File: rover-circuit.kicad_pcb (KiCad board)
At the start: 2 copper layers, 78 x 75.3 mm, 86 parts, among them J1 Battery Connector, J2 USB_C_Receptacle_USB2.0_14P, J3 Conn_01x04, J4 Conn_01x04_Socket, J5 Raspberry_Pi_2_3, J6 Conn_02x07_Odd_Even, M1 Motor_DC, M2 Motor_DC, SW1 SW_EN, SW2 SW_IO0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

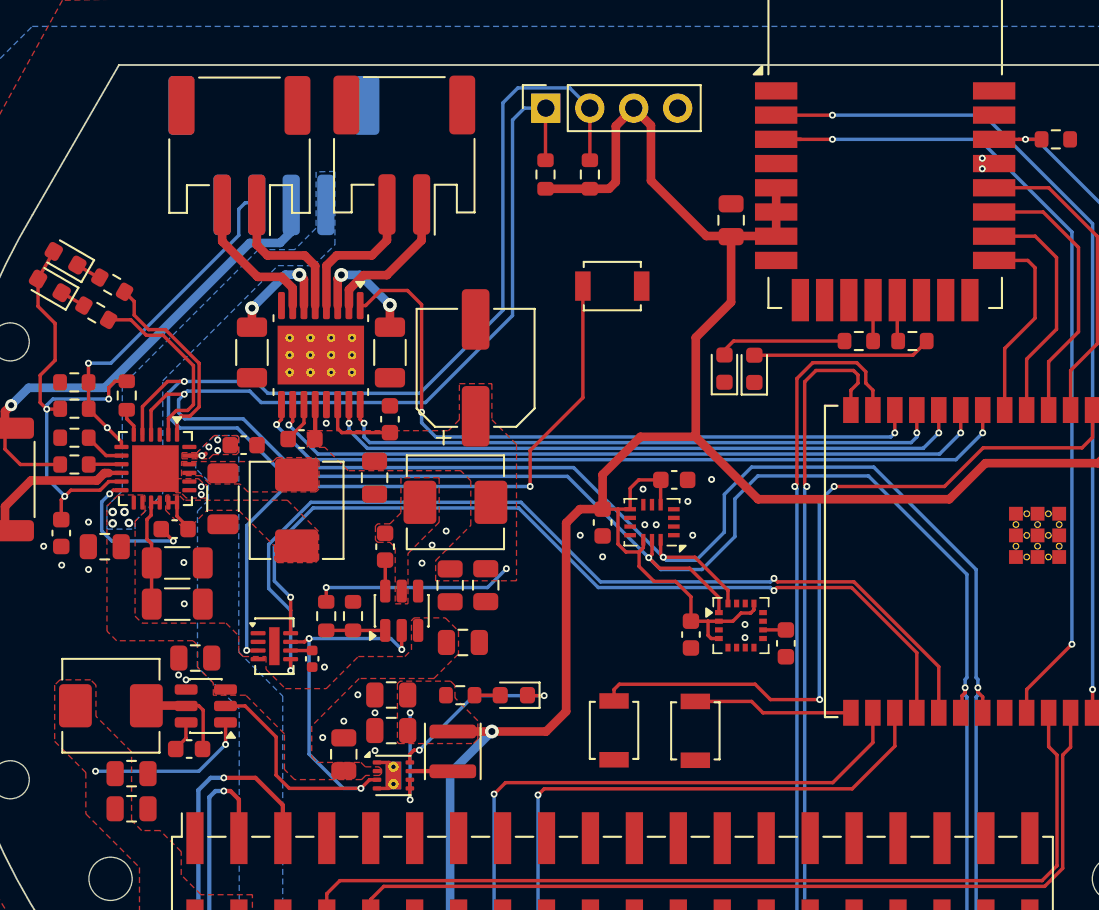
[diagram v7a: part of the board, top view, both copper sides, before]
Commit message: improved routing
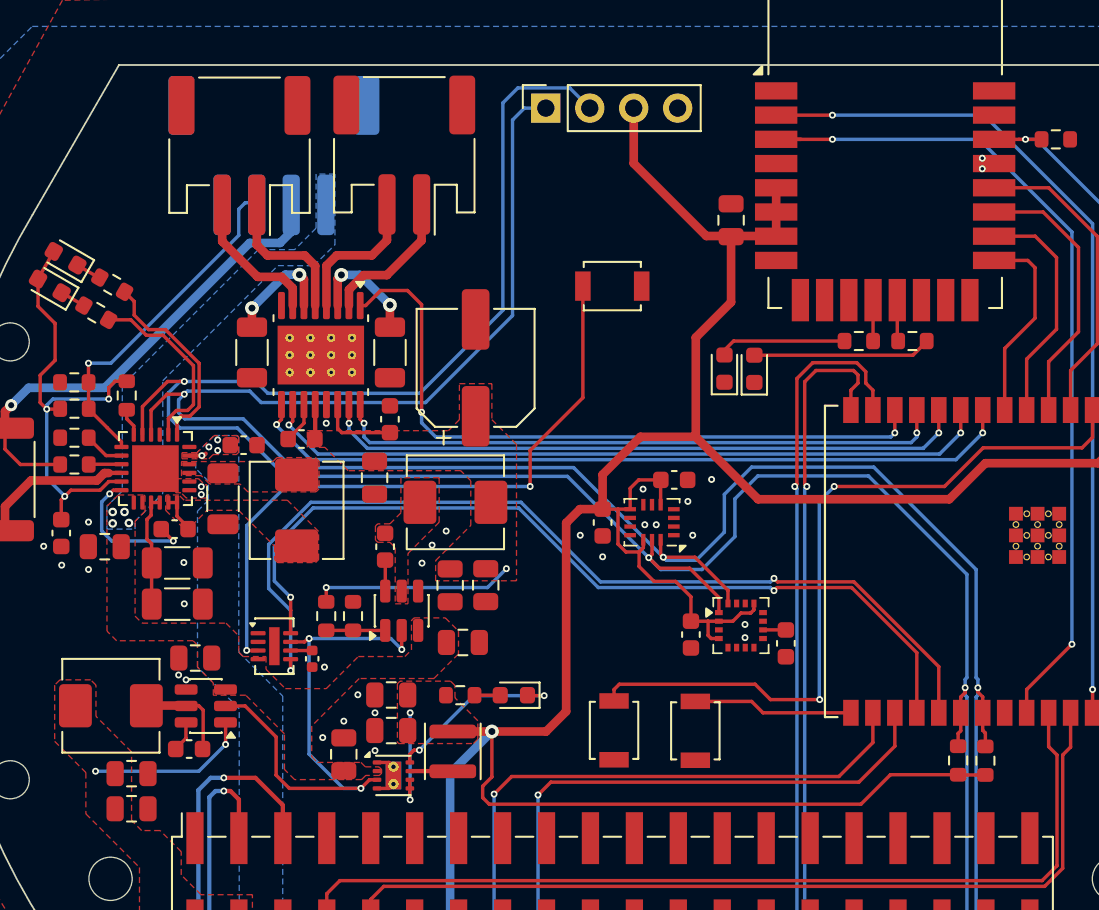
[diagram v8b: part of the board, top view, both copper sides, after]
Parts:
- moved R16 42.4 mm to (178.8, 97.5)
- moved R17 40.0 mm to (177.2, 97.5)
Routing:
- net +3V3: track 174.2 -> 199.3 mm
- net /Battery Recharger/SCL: track 161.9 -> 160.9 mm
- net /Battery Recharger/SDA: track 157.9 -> 156.9 mm
- net /Battery Recharger/TS: vias 2 -> 1
